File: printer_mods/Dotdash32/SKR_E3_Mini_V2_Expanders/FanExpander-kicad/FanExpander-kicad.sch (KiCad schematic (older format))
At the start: 66 parts, among them J0 FAN0, J1 FAN1, J10 FAN0_IN, J12 HI_PWR2, J2 FAN2, J3 FAN3, J4 FAN4, J5 FAN5, J6 FAN6, J7 FAN7, J8 EXP1_IN, J9 5V_In, Q1 IRLML6344, Q2 IRLML6344, Q3 IRLML6344, Q4 IRLML6344, Q5 IRLML6344, Q6 IRLML6344, Q7 IRLML6344

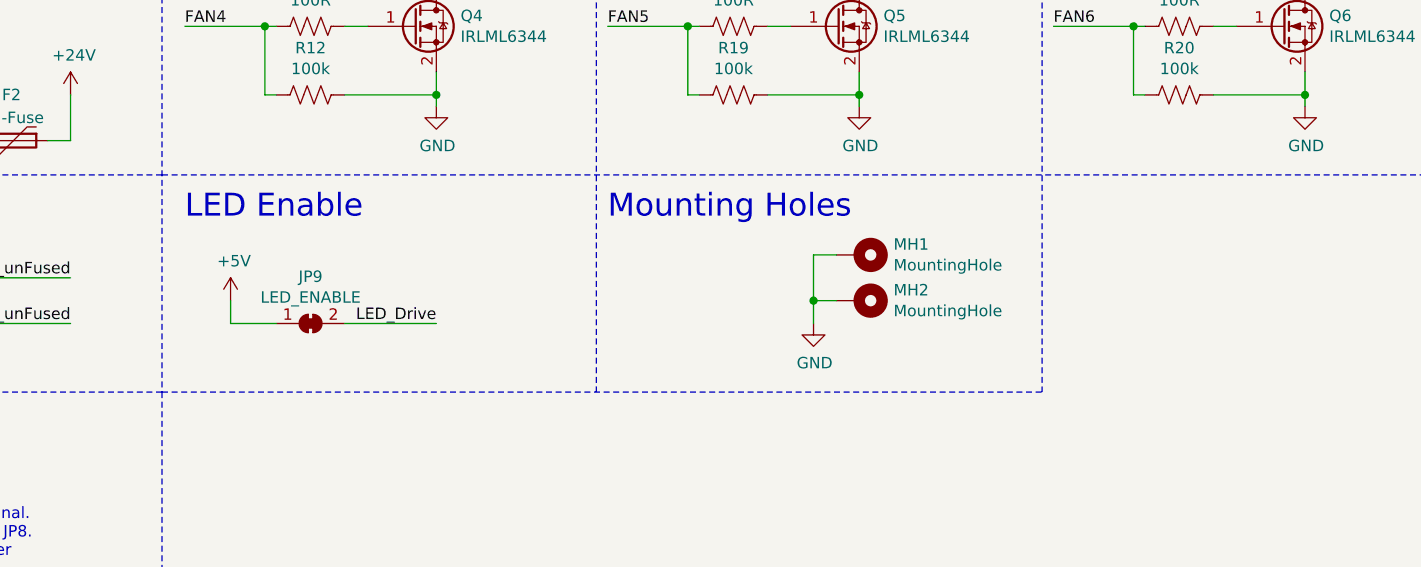
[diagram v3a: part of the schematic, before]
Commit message: chore: updating layout to new method, new LED
new LED reverse mount footprint, should be slightly less bulky
and make sure all the light just goes up through JST connector
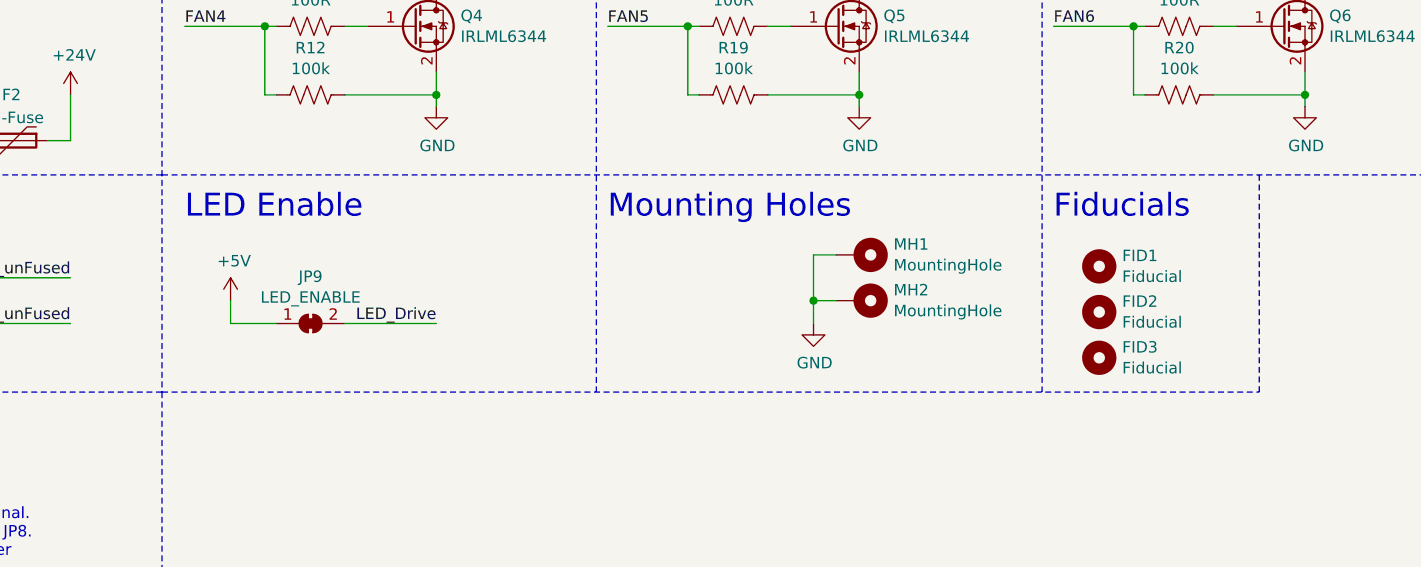
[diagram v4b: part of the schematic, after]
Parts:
- added FID1, FID2, FID3: Fiducial, Fiducials:Fiducial_0.5mm_Dia_1mm_Outer, symbol Mechanical:MountingHole
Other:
- note added: "Fiducials"
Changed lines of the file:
@@
 Wire Notes Line width 12 style solid
 	3000 500  3000 5250
-Wire Notes Line
-	3000 5250 6850 5250
 Text Label 1950 2700 2    50   ~ 0
 5V_EXP
@@
 Wire Notes Line
 	3000 6400 500  6400
+$Comp
+L Mechanical:MountingHole FID1
+U 1 1 62078A04
+P 7100 4700
+F 0 "FID1" H 7200 4746 50  0000 L CNN
+F 1 "Fiducial" H 7200 4655 50  0000 L CNN
+F 2 "Fiducials:Fiducial_0.5mm_Dia_1mm_Outer" H 7100 4700 50  0001 C CNN
+F 3 "~" H 7100 4700 50  0001 C CNN
+	1    7100 4700
+	1    0    0    -1
+$EndComp
+$Comp
+L Mechanical:MountingHole FID2
+U 1 1 62080AE9
+P 7100 4900
+F 0 "FID2" H 7200 4946 50  0000 L CNN
+F 1 "Fiducial" H 7200 4855 50  0000 L CNN
+F 2 "Fiducials:Fiducial_0.5mm_Dia_1mm_Outer" H 7100 4900 50  0001 C CNN
+F 3 "~" H 7100 4900 50  0001 C CNN
+	1    7100 4900
+	1    0    0    -1
+$EndComp
+$Comp
+L Mechanical:MountingHole FID3
+U 1 1 6208B033
+P 7100 5100
+F 0 "FID3" H 7200 5146 50  0000 L CNN
+F 1 "Fiducial" H 7200 5055 50  0000 L CNN
+F 2 "Fiducials:Fiducial_0.5mm_Dia_1mm_Outer" H 7100 5100 50  0001 C CNN
+F 3 "~" H 7100 5100 50  0001 C CNN
+	1    7100 5100
+	1    0    0    -1
+$EndComp
+Text Notes 6900 4500 0    100  ~ 0
+Fiducials
+Wire Notes Line
+	7800 5250 7800 4300
+Wire Notes Line
+	3000 5250 7800 5250
 $EndSCHEMATC

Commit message: chore: changing values for BOM export
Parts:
- D1, D2, D3, D4, D5, D6, D7, D8: footprint LED_SMD:LED_1206_3216Metric_ReverseMount_Hole1.8x2.4mm -> LED_SMD:LED_1206_3216Metric_ReverseMount_Hole2.1x2.1mm
- F1, F2: symbol Device:Polyfuse -> Device:Fuse
- J0: value FAN0 -> JST-XH2
- J1: value FAN1 -> JST-XH2
- J10: value FAN0_IN -> JST-XH2
- J2: value FAN2 -> JST-XH2
- J3: value FAN3 -> JST-XH2
- J4: value FAN4 -> JST-XH2
- J5: value FAN5 -> JST-XH2
- J6: value FAN6 -> JST-XH2
- J7: value FAN7 -> JST-XH2
- J8: value EXP1_IN -> EXPx_IN
- JP0: value V_SELECT0 -> V_SELECT
- JP1: value V_SELECT1 -> V_SELECT
- JP2: value V_SELECT2 -> V_SELECT
- JP3: value V_SELECT3 -> V_SELECT
- JP4: value V_SELECT4 -> V_SELECT
- JP5: value V_SELECT5 -> V_SELECT
- JP6: value V_SELECT6 -> V_SELECT
- JP7: value V_SELECT7 -> V_SELECT
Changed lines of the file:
@@
 Sheet 1 1
 Title "SKR Fan Expander"
-Date "2022-01-01"
-Rev "V0.1.3"
+Date "2022-01-11"
+Rev "V0.1.4"
 Comp "Voron Design"
 Comment1 "Drawn by Dotdash32 (JDeW)"
@@
 P 10200 1350
 F 0 "J3" H 10280 1342 50  0000 L CNN
-F 1 "FAN3" H 10280 1251 50  0000 L CNN
+F 1 "JST-XH2" H 10280 1251 50  0000 L CNN
 F 2 "Connectors_JST:JST_XH_B02B-XH-A_02x2.50mm_Straight" H 10200 1350 50  0001 C CNN
 F 3 "~" H 10200 1350 50  0001 C CNN
@@
 P 9650 1200
 F 0 "JP3" H 9700 1400 50  0000 R CNN
-F 1 "V_SELECT3" H 9850 1300 50  0000 R CNN
+F 1 "V_SELECT" H 9850 1300 50  0000 R CNN
 F 2 "Pin_Headers:Pin_Header_Straight_1x03_Pitch2.54mm" H 9650 1200 50  0001 C CNN
 F 3 "~" H 9650 1200 50  0001 C CNN
@@
 F 0 "D5" V 9339 1433 50  0000 R CNN
 F 1 "LED" V 9248 1433 50  0000 R CNN
-F 2 "LED_SMD:LED_1206_3216Metric_ReverseMount_Hole1.8x2.4mm" H 9300 1550 50  0001 C CNN
+F 2 "LED_SMD:LED_1206_3216Metric_ReverseMount_Hole2.1x2.1mm" H 9300 1550 50  0001 C CNN
 F 3 "~" H 9300 1550 50  0001 C CNN
 	1    9300 1550
@@
 P 4550 3100
 F 0 "J4" H 4630 3092 50  0000 L CNN
-F 1 "FAN4" H 4630 3001 50  0000 L CNN
+F 1 "JST-XH2" H 4630 3001 50  0000 L CNN
 F 2 "Connectors_JST:JST_XH_B02B-XH-A_02x2.50mm_Straight" H 4550 3100 50  0001 C CNN
 F 3 "~" H 4550 3100 50  0001 C CNN
@@
 P 4000 2950
 F 0 "JP4" H 4050 3150 50  0000 R CNN
-F 1 "V_SELECT4" H 4200 3050 50  0000 R CNN
+F 1 "V_SELECT" H 4200 3050 50  0000 R CNN
 F 2 "Pin_Headers:Pin_Header_Straight_1x03_Pitch2.54mm" H 4000 2950 50  0001 C CNN
 F 3 "~" H 4000 2950 50  0001 C CNN
@@
 F 0 "D6" V 3689 3183 50  0000 R CNN
 F 1 "LED" V 3598 3183 50  0000 R CNN
-F 2 "LED_SMD:LED_1206_3216Metric_ReverseMount_Hole1.8x2.4mm" H 3650 3300 50  0001 C CNN
+F 2 "LED_SMD:LED_1206_3216Metric_ReverseMount_Hole2.1x2.1mm" H 3650 3300 50  0001 C CNN
 F 3 "~" H 3650 3300 50  0001 C CNN
 	1    3650 3300
@@
 F 0 "D7" V 5539 3183 50  0000 R CNN
 F 1 "LED" V 5448 3183 50  0000 R CNN
-F 2 "LED_SMD:LED_1206_3216Metric_ReverseMount_Hole1.8x2.4mm" H 5500 3300 50  0001 C CNN
+F 2 "LED_SMD:LED_1206_3216Metric_ReverseMount_Hole2.1x2.1mm" H 5500 3300 50  0001 C CNN
 F 3 "~" H 5500 3300 50  0001 C CNN
 	1    5500 3300
@@
 P 6400 3100
 F 0 "J5" H 6480 3092 50  0000 L CNN
-F 1 "FAN5" H 6480 3001 50  0000 L CNN
+F 1 "JST-XH2" H 6480 3001 50  0000 L CNN
 F 2 "Connectors_JST:JST_XH_B02B-XH-A_02x2.50mm_Straight" H 6400 3100 50  0001 C CNN
 F 3 "~" H 6400 3100 50  0001 C CNN
@@
 P 1050 1650
 F 0 "J8" H 1100 2067 50  0000 C CNN
-F 1 "EXP1_IN" H 1100 1976 50  0000 C CNN
+F 1 "EXPx_IN" H 1100 1976 50  0000 C CNN
 F 2 "Connectors_Multicomp:Multicomp_MC9A12-1034_2x05x2.54mm_Straight" H 1050 1650 50  0001 C CNN
 F 3 "~" H 1050 1650 50  0001 C CNN
@@
 P 5850 2950
 F 0 "JP5" H 5900 3150 50  0000 R CNN
-F 1 "V_SELECT5" H 6050 3050 50  0000 R CNN
+F 1 "V_SELECT" H 6050 3050 50  0000 R CNN
 F 2 "Pin_Headers:Pin_Header_Straight_1x03_Pitch2.54mm" H 5850 2950 50  0001 C CNN
 F 3 "~" H 5850 2950 50  0001 C CNN
@@
 F 0 "D1" V 5589 1483 50  0000 R CNN
 F 1 "LED" V 5498 1483 50  0000 R CNN
-F 2 "LED_SMD:LED_1206_3216Metric_ReverseMount_Hole1.8x2.4mm" H 5550 1600 50  0001 C CNN
+F 2 "LED_SMD:LED_1206_3216Metric_ReverseMount_Hole2.1x2.1mm" H 5550 1600 50  0001 C CNN
 F 3 "~" H 5550 1600 50  0001 C CNN
 	1    5550 1600
@@
 P 6450 1400
 F 0 "J1" H 6530 1392 50  0000 L CNN
-F 1 "FAN1" H 6530 1301 50  0000 L CNN
+F 1 "JST-XH2" H 6530 1301 50  0000 L CNN
 F 2 "Connectors_JST:JST_XH_B02B-XH-A_02x2.50mm_Straight" H 6450 1400 50  0001 C CNN
 F 3 "~" H 6450 1400 50  0001 C CNN
@@
 P 5900 1250
 F 0 "JP1" H 5950 1450 50  0000 R CNN
-F 1 "V_SELECT1" H 6100 1350 50  0000 R CNN
+F 1 "V_SELECT" H 6100 1350 50  0000 R CNN
 F 2 "Pin_Headers:Pin_Header_Straight_1x03_Pitch2.54mm" H 5900 1250 50  0001 C CNN
 F 3 "~" H 5900 1250 50  0001 C CNN
@@
 F 0 "D4" V 7539 1433 50  0000 R CNN
 F 1 "LED" V 7448 1433 50  0000 R CNN
-F 2 "LED_SMD:LED_1206_3216Metric_ReverseMount_Hole1.8x2.4mm" H 7500 1550 50  0001 C CNN
+F 2 "LED_SMD:LED_1206_3216Metric_ReverseMount_Hole2.1x2.1mm" H 7500 1550 50  0001 C CNN
 F 3 "~" H 7500 1550 50  0001 C CNN
 	1    7500 1550
@@
 P 7850 1200
 F 0 "JP2" H 7900 1400 50  0000 R CNN
-F 1 "V_SELECT2" H 8050 1300 50  0000 R CNN
+F 1 "V_SELECT" H 8050 1300 50  0000 R CNN
 F 2 "Pin_Headers:Pin_Header_Straight_1x03_Pitch2.54mm" H 7850 1200 50  0001 C CNN
 F 3 "~" H 7850 1200 50  0001 C CNN
@@
 P 8400 1350
 F 0 "J2" H 8480 1342 50  0000 L CNN
-F 1 "FAN2" H 8480 1251 50  0000 L CNN
+F 1 "JST-XH2" H 8480 1251 50  0000 L CNN
 F 2 "Connectors_JST:JST_XH_B02B-XH-A_02x2.50mm_Straight" H 8400 1350 50  0001 C CNN
 F 3 "~" H 8400 1350 50  0001 C CNN
@@
 P 650 4150
 F 0 "J10" H 568 3825 50  0000 C CNN
-F 1 "FAN0_IN" H 568 3916 50  0000 C CNN
+F 1 "JST-XH2" H 568 3916 50  0000 C CNN
 F 2 "Connectors_JST:JST_XH_B02B-XH-A_02x2.50mm_Straight" H 650 4150 50  0001 C CNN
 F 3 "~" H 650 4150 50  0001 C CNN
@@
 FAN0_Dr
 $Comp
-L Device:Polyfuse F2
+L Device:Fuse F2
 U 1 1 61CA0A67
 P 2350 4150
@@
 P 7800 2950
 F 0 "JP6" H 7850 3150 50  0000 R CNN
-F 1 "V_SELECT6" H 8000 3050 50  0000 R CNN
+F 1 "V_SELECT" H 8000 3050 50  0000 R CNN
 F 2 "Pin_Headers:Pin_Header_Straight_1x03_Pitch2.54mm" H 7800 2950 50  0001 C CNN
 F 3 "~" H 7800 2950 50  0001 C CNN
@@
 P 8350 3100
 F 0 "J6" H 8430 3092 50  0000 L CNN
-F 1 "FAN6" H 8430 3001 50  0000 L CNN
+F 1 "JST-XH2" H 8430 3001 50  0000 L CNN
 F 2 "Connectors_JST:JST_XH_B02B-XH-A_02x2.50mm_Straight" H 8350 3100 50  0001 C CNN
 F 3 "~" H 8350 3100 50  0001 C CNN
@@
 F 0 "D8" V 7489 3183 50  0000 R CNN
 F 1 "LED" V 7398 3183 50  0000 R CNN
-F 2 "LED_SMD:LED_1206_3216Metric_ReverseMount_Hole1.8x2.4mm" H 7450 3300 50  0001 C CNN
+F 2 "LED_SMD:LED_1206_3216Metric_ReverseMount_Hole2.1x2.1mm" H 7450 3300 50  0001 C CNN
 F 3 "~" H 7450 3300 50  0001 C CNN
 	1    7450 3300
@@
 F 0 "D2" V 9339 3183 50  0000 R CNN
 F 1 "LED" V 9248 3183 50  0000 R CNN
-F 2 "LED_SMD:LED_1206_3216Metric_ReverseMount_Hole1.8x2.4mm" H 9300 3300 50  0001 C CNN
+F 2 "LED_SMD:LED_1206_3216Metric_ReverseMount_Hole2.1x2.1mm" H 9300 3300 50  0001 C CNN
 F 3 "~" H 9300 3300 50  0001 C CNN
 	1    9300 3300
@@
 P 10200 3100
 F 0 "J7" H 10280 3092 50  0000 L CNN
-F 1 "FAN7" H 10280 3001 50  0000 L CNN
+F 1 "JST-XH2" H 10280 3001 50  0000 L CNN
 F 2 "Connectors_JST:JST_XH_B02B-XH-A_02x2.50mm_Straight" H 10200 3100 50  0001 C CNN
 F 3 "~" H 10200 3100 50  0001 C CNN
@@
 P 9650 2950
 F 0 "JP7" H 9700 3150 50  0000 R CNN
-F 1 "V_SELECT7" H 9850 3050 50  0000 R CNN
+F 1 "V_SELECT" H 9850 3050 50  0000 R CNN
 F 2 "Pin_Headers:Pin_Header_Straight_1x03_Pitch2.54mm" H 9650 2950 50  0001 C CNN
 F 3 "~" H 9650 2950 50  0001 C CNN
@@
 F 0 "D3" V 3689 1483 50  0000 R CNN
 F 1 "LED" V 3598 1483 50  0000 R CNN
-F 2 "LED_SMD:LED_1206_3216Metric_ReverseMount_Hole1.8x2.4mm" H 3650 1600 50  0001 C CNN
+F 2 "LED_SMD:LED_1206_3216Metric_ReverseMount_Hole2.1x2.1mm" H 3650 1600 50  0001 C CNN
 F 3 "~" H 3650 1600 50  0001 C CNN
 	1    3650 1600
@@
 P 4550 1400
 F 0 "J0" H 4630 1392 50  0000 L CNN
-F 1 "FAN0" H 4630 1301 50  0000 L CNN
+F 1 "JST-XH2" H 4630 1301 50  0000 L CNN
 F 2 "Connectors_JST:JST_XH_B02B-XH-A_02x2.50mm_Straight" H 4550 1400 50  0001 C CNN
 F 3 "~" H 4550 1400 50  0001 C CNN
@@
 P 4000 1250
 F 0 "JP0" H 4050 1450 50  0000 R CNN
-F 1 "V_SELECT0" H 4200 1350 50  0000 R CNN
+F 1 "V_SELECT" H 4200 1350 50  0000 R CNN
 F 2 "Pin_Headers:Pin_Header_Straight_1x03_Pitch2.54mm" H 4000 1250 50  0001 C CNN
 F 3 "~" H 4000 1250 50  0001 C CNN
@@
 	2500 3100 2650 3100
 $Comp
-L Device:Polyfuse F1
+L Device:Fuse F1
 U 1 1 61C255C6
 P 2350 3100

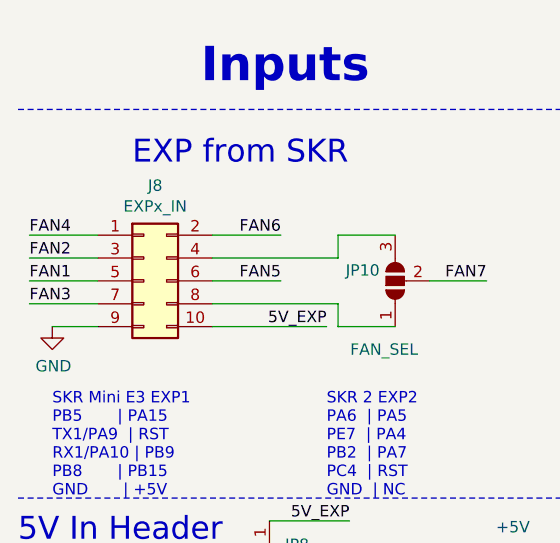
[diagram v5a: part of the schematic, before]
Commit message: feat: initial routing of FE beefy boi
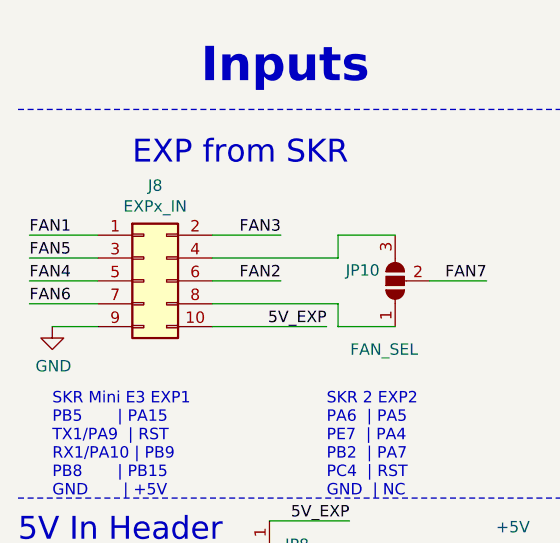
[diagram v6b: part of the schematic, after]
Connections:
- net FAN1: now also J8.1 (Pin_1); no longer J8.5 (Pin_5)
- net FAN2: now also J8.6 (Pin_6); no longer J8.3 (Pin_3)
- net FAN3: now also J8.2 (Pin_2); no longer J8.7 (Pin_7)
- net FAN4: now also J8.5 (Pin_5); no longer J8.1 (Pin_1)
- net FAN5: now also J8.3 (Pin_3); no longer J8.6 (Pin_6)
- net FAN6: now also J8.7 (Pin_7); no longer J8.2 (Pin_2)
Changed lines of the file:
@@
 Wire Wire Line
 	550  1450 850  1450
+Text Label 550  1450 0    50   ~ 0
+FAN1
+Wire Wire Line
+	850  1550 550  1550
+Wire Wire Line
+	850  1650 550  1650
+Wire Wire Line
+	550  1750 850  1750
+Wire Wire Line
+	1350 1450 1650 1450
+Wire Wire Line
+	1350 1650 1650 1650
+Text Label 1650 1650 2    50   ~ 0
+FAN2
+Text Label 1650 1450 2    50   ~ 0
+FAN3
 Text Label 550  1650 0    50   ~ 0
-FAN1
-Wire Wire Line
-	850  1550 550  1550
-Wire Wire Line
-	850  1650 550  1650
-Wire Wire Line
-	550  1750 850  1750
-Wire Wire Line
-	1350 1450 1650 1450
-Wire Wire Line
-	1350 1650 1650 1650
+FAN4
 Text Label 550  1550 0    50   ~ 0
-FAN2
-Text Label 550  1750 0    50   ~ 0
-FAN3
-Text Label 550  1450 0    50   ~ 0
-FAN4
-Text Label 1650 1650 2    50   ~ 0
 FAN5
 $Comp
@@
 Wire Wire Line
 	1350 1550 1900 1550
-Text Label 1650 1450 2    50   ~ 0
+Text Label 550  1750 0    50   ~ 0
 FAN6
 Text Label 2550 1650 2    50   ~ 0

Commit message: feat: prep big expander for release
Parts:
- added JP13: 5V_Term, Jumper:SolderJumper-2_P1.3mm_Open_RoundedPad1.0x1.5mm, symbol Jumper:SolderJumper_2_Open
- added JP14: 24V_Term, Jumper:SolderJumper-2_P1.3mm_Open_RoundedPad1.0x1.5mm, symbol Jumper:SolderJumper_2_Open
- JP11, JP8, JP9: footprint Jumper:SolderJumper-2_P1.3mm_Bridged_RoundedPad1.0x1.5mm -> Jumper:SolderJumper-2_P1.3mm_Pasted_RoundedPad1.0x1.5mm
- JP12: footprint Jumper:SolderJumper-2_P1.3mm_Bridged2Bar_RoundedPad1.0x1.5mm -> Jumper:SolderJumper-2_P1.3mm_Open_RoundedPad1.0x1.5mm
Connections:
- net 24V_unFused: now also JP14.2 (B); no longer J12.1 (Pin_1)
- net 5V_unFused: now also JP13.2 (B); no longer J12.3 (Pin_3)
- new net 24v_Screw: J12.1 (Pin_1), JP14.1 (A)
- new net 5V_Screw: J12.3 (Pin_3), JP13.1 (A)
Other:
- moved on the sheet: J12
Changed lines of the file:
@@
 Sheet 1 1
 Title "SKR Fan Expander"
-Date "2022-01-14"
-Rev "V0.1.5"
+Date "2022-01-16"
+Rev "V1.0.1"
 Comp "Voron Design"
 Comment1 "Drawn by Dotdash32 (JDeW)"
@@
 F 0 "JP9" H 3650 5155 50  0000 C CNN
 F 1 "LED_ENABLE" H 3650 5064 50  0000 C CNN
-F 2 "Jumper:SolderJumper-2_P1.3mm_Bridged_RoundedPad1.0x1.5mm" H 3650 4950 50  0001 C CNN
+F 2 "Jumper:SolderJumper-2_P1.3mm_Pasted_RoundedPad1.0x1.5mm" H 3650 4950 50  0001 C CNN
 F 3 "~" H 3650 4950 50  0001 C CNN
 	1    3650 4950
@@
 Connection ~ 5850 4850
 Wire Notes Line
-	4900 900  4900 5250
+	4900 900  4900 5350
 Wire Notes Line
-	6850 900  6850 5250
+	6850 1050 6850 5350
 Text Notes 4950 4500 0    100  ~ 0
 Mounting Holes
@@
 	3000 4300 500  4300
 Wire Notes Line width 12 style solid
-	3000 5250 500  5250
+	3000 5350 500  5350
 Wire Notes Line width 12 style solid
-	3000 500  3000 5250
+	3000 500  3000 5350
 Text Label 1950 2700 2    50   ~ 0
 5V_EXP
@@
 F 0 "JP8" V 1554 2918 50  0000 L CNN
 F 1 "5V_EXP_CONN" V 1645 2918 50  0000 L CNN
-F 2 "Jumper:SolderJumper-2_P1.3mm_Bridged_RoundedPad1.0x1.5mm" H 1600 2850 50  0001 C CNN
+F 2 "Jumper:SolderJumper-2_P1.3mm_Pasted_RoundedPad1.0x1.5mm" H 1600 2850 50  0001 C CNN
 F 3 "~" H 1600 2850 50  0001 C CNN
 	1    1600 2850
@@
 F 0 "JP12" H 4500 2055 50  0000 C CNN
 F 1 "FAN0_CTRL" H 4500 1964 50  0000 C CNN
-F 2 "Jumper:SolderJumper-2_P1.3mm_Bridged2Bar_RoundedPad1.0x1.5mm" H 4500 1850 50  0001 C CNN
+F 2 "Jumper:SolderJumper-2_P1.3mm_Open_RoundedPad1.0x1.5mm" H 4500 1850 50  0001 C CNN
 F 3 "~" H 4500 1850 50  0001 C CNN
 	1    4500 1850
@@
 L Connector_Generic:Conn_01x03 J12
 U 1 1 61F3F4E8
-P 1800 4850
-F 0 "J12" H 1718 4525 50  0000 C CNN
-F 1 "HI_PWR2" H 1718 4616 50  0000 C CNN
-F 2 "TerminalBlock_Pheonix:TerminalBlock_Phoenix_MKDS-1,5-3-5.08_1x03_P5.08mm_Horizontal" H 1800 4850 50  0001 C CNN
-F 3 "~" H 1800 4850 50  0001 C CNN
-	1    1800 4850
+P 1250 4900
+F 0 "J12" H 1168 4575 50  0000 C CNN
+F 1 "HI_PWR2" H 1168 4666 50  0000 C CNN
+F 2 "TerminalBlock_Pheonix:TerminalBlock_Phoenix_MKDS-1,5-3-5.08_1x03_P5.08mm_Horizontal" H 1250 4900 50  0001 C CNN
+F 3 "~" H 1250 4900 50  0001 C CNN
+	1    1250 4900
 	-1   0    0    1
 $EndComp
@@
 L power:GND #PWR0108
 U 1 1 61FA64D9
-P 2050 5000
-F 0 "#PWR0108" H 2050 4750 50  0001 C CNN
-F 1 "GND" H 2055 4827 50  0000 C CNN
-F 2 "" H 2050 5000 50  0001 C CNN
-F 3 "" H 2050 5000 50  0001 C CNN
-	1    2050 5000
-	1    0    0    -1
-$EndComp
-Wire Wire Line
-	2000 4850 2050 4850
-Wire Wire Line
-	2000 4950 2600 4950
-Wire Wire Line
-	2000 4750 2600 4750
-Text Label 2600 4750 2    50   ~ 0
+P 1500 5050
+F 0 "#PWR0108" H 1500 4800 50  0001 C CNN
+F 1 "GND" H 1505 4877 50  0000 C CNN
+F 2 "" H 1500 5050 50  0001 C CNN
+F 3 "" H 1500 5050 50  0001 C CNN
+	1    1500 5050
+	1    0    0    -1
+$EndComp
+Wire Wire Line
+	1450 4900 1500 4900
+Text Label 2900 4700 2    50   ~ 0
 5V_unFused
-Text Label 2600 4950 2    50   ~ 0
+Text Label 2900 5050 2    50   ~ 0
 24V_unFused
 Wire Wire Line
-	2050 5000 2050 4850
-Text Notes 550  6300 0    50   ~ 0
+	1500 5050 1500 4900
+Text Notes 550  6400 0    50   ~ 0
 Power should be supplied to only \n1 (ONE) input per voltage level.\n\n5V comes from EXP, 5V header, or 5V Screw Terminal.\n  If using 5V Header/Screw Terminal and EXP1, cut JP8.\n  If using Screw Terminal, do not connect 5V Header\n\n24V comes from Fan0 In or 24V Screw Terminal\n  If using Screw Terminal, cut JP11\n  JP12 can be closed to make Fan0 Always On
 $Comp
@@
 F 0 "JP11" H 1350 4350 50  0000 L CNN
 F 1 "Fan0_PWR" H 1250 4250 50  0000 L CNN
-F 2 "Jumper:SolderJumper-2_P1.3mm_Bridged_RoundedPad1.0x1.5mm" H 1400 4150 50  0001 C CNN
+F 2 "Jumper:SolderJumper-2_P1.3mm_Pasted_RoundedPad1.0x1.5mm" H 1400 4150 50  0001 C CNN
 F 3 "~" H 1400 4150 50  0001 C CNN
 	1    1400 4150
@@
 Text Label 900  4150 0    50   ~ 0
 24V_F0
-Text Notes 550  5450 0    100  ~ 0
+Text Notes 550  5550 0    100  ~ 0
 Notes on Power Input
 Wire Notes Line
-	3000 5250 3000 6400
+	3000 5250 3000 6500
 Wire Notes Line
-	3000 6400 500  6400
+	3000 6500 500  6500
 $Comp
 L Mechanical:MountingHole FID1
@@
 Fiducials
 Wire Notes Line
-	7800 5250 7800 4300
+	7800 5350 7800 4300
 Wire Notes Line
-	3000 5250 7800 5250
+	3000 5350 7800 5350
+$Comp
+L Jumper:SolderJumper_2_Open JP13
+U 1 1 61EEFF27
+P 2250 4700
+F 0 "JP13" H 2250 4905 50  0000 C CNN
+F 1 "5V_Term" H 2250 4814 50  0000 C CNN
+F 2 "Jumper:SolderJumper-2_P1.3mm_Open_RoundedPad1.0x1.5mm" H 2250 4700 50  0001 C CNN
+F 3 "~" H 2250 4700 50  0001 C CNN
+	1    2250 4700
+	1    0    0    -1
+$EndComp
+$Comp
+L Jumper:SolderJumper_2_Open JP14
+U 1 1 61EF10E8
+P 2250 5050
+F 0 "JP14" H 2250 5255 50  0000 C CNN
+F 1 "24V_Term" H 2250 5164 50  0000 C CNN
+F 2 "Jumper:SolderJumper-2_P1.3mm_Open_RoundedPad1.0x1.5mm" H 2250 5050 50  0001 C CNN
+F 3 "~" H 2250 5050 50  0001 C CNN
+	1    2250 5050
+	1    0    0    -1
+$EndComp
+Wire Wire Line
+	2900 4700 2400 4700
+Wire Wire Line
+	1450 5000 1700 5000
+Wire Wire Line
+	1700 5000 1700 5050
+Wire Wire Line
+	1700 5050 2100 5050
+Wire Wire Line
+	1450 4800 1700 4800
+Wire Wire Line
+	1700 4800 1700 4700
+Wire Wire Line
+	1700 4700 2100 4700
+Wire Wire Line
+	2400 5050 2900 5050
+Text Label 1700 4700 0    50   ~ 0
+5V_Screw
+Text Label 1700 5050 0    50   ~ 0
+24v_Screw
 $EndSCHEMATC
